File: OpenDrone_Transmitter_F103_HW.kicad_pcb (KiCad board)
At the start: 2 copper layers, 62 x 37 mm, 87 parts, among them J1 Conn_01x03, J10 Conn_01x04, J11 Conn_01x03, J12 Conn_01x04, J13 Conn_01x02, J14 Conn_01x05, J15 Conn_01x02, J16 Conn_02x04_Odd_Even, J17 Conn_01x02, J18 Conn_01x02, J19 Conn_01x03, J2 Conn_01x05, J20 Conn_01x02, J21 Conn_01x02, J22 Conn_01x02, J23 Conn_01x08, J3 Conn_01x03, J4 Conn_01x03, J5 Conn_01x03, J6 Conn_01x02, J7 Conn_01x02, J8 Conn_01x03, J9 Conn_01x03, SW1 RESET, U1 STM32F103C8Tx, U2 AMS1117-3.3, U3 TPS54331, Y2 Crystal_GND24

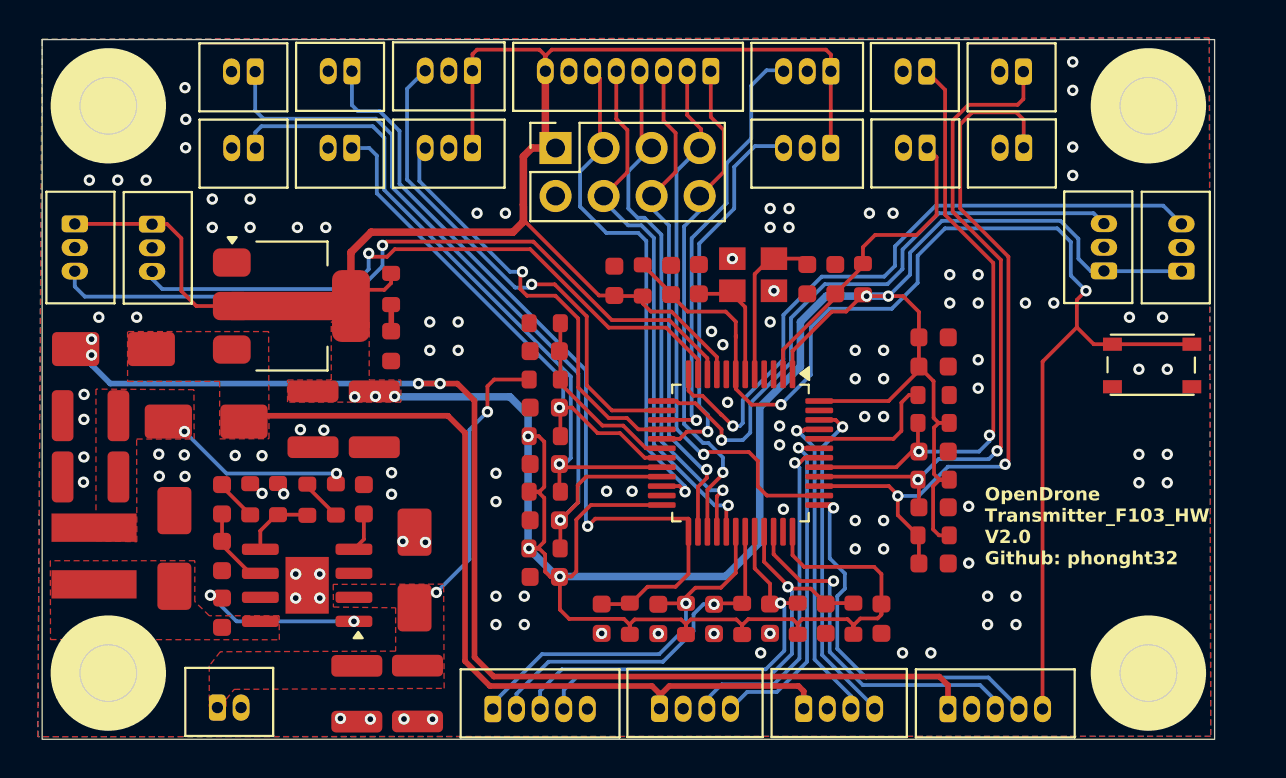
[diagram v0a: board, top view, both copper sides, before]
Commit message: update board size
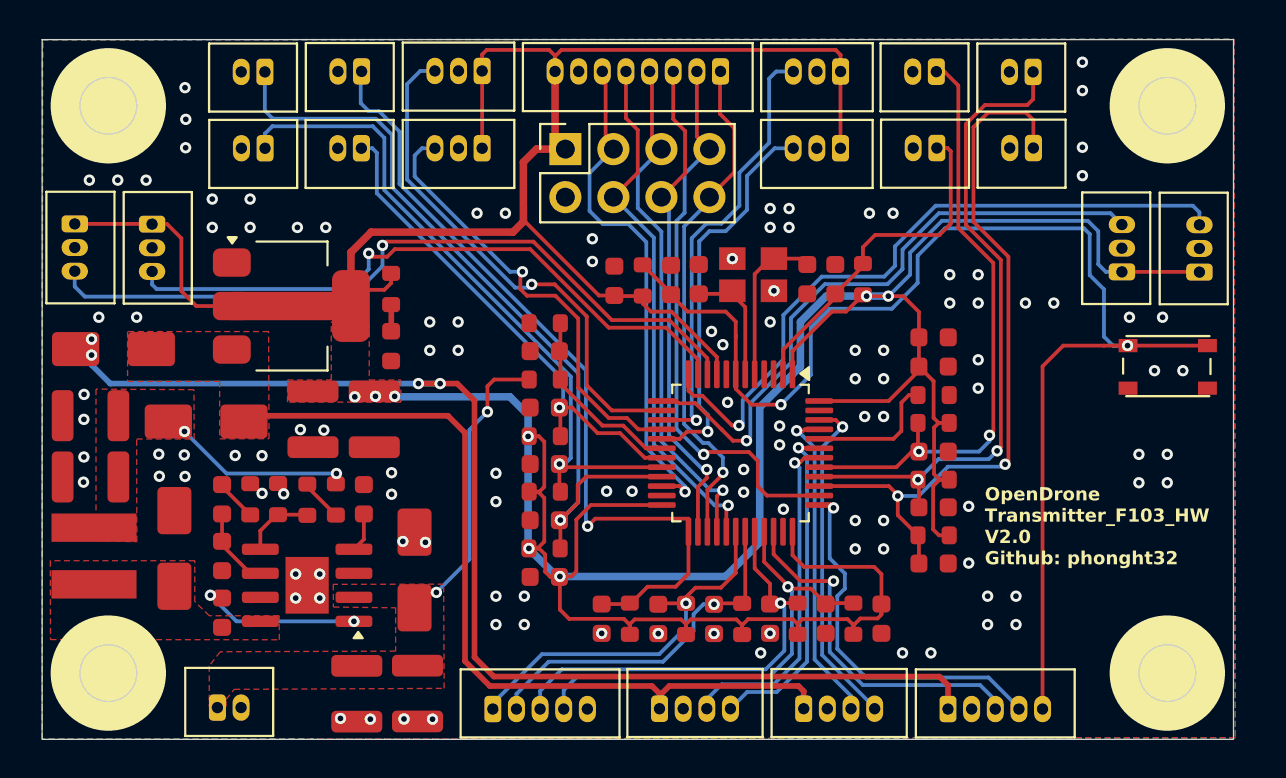
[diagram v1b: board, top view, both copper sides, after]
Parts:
- moved J19 0.95 mm to (224.7, 84.4)
- moved J5 0.95 mm to (220.6, 84.3)
- moved SW1 0.83 mm to (223.0, 89.4)
- moved J16 0.52 mm to (191.2, 77.9)
- moved J1 0.51 mm to (205.7, 73.8)
- moved J15 0.51 mm to (215.9, 73.8)
- moved J21 0.51 mm to (215.9, 77.8)
- moved J22 0.51 mm to (210.8, 77.8)
- moved J23 0.51 mm to (199.4, 73.8)
- moved J6 0.51 mm to (180.4, 73.8)
- moved J13 0.51 mm to (175.3, 77.8)
- moved J18 0.51 mm to (210.8, 73.8)
- moved J8 0.51 mm to (186.8, 73.7)
- moved J9 0.51 mm to (186.8, 77.8)
- moved J17 0.51 mm to (175.3, 73.8)
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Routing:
- net STM32_RESET: track 66.9 -> 69.8 mm
- net +3V3: track 240.6 -> 242.3 mm
- net PC13: track 16.7 -> 18.1 mm
- net RIGHT_JOYSTICK_IN1: track 35.6 -> 37.0 mm
- net VOLUME_3: track 23.0 -> 23.8 mm
- net RIGHT_JOYSTICK_IN2: track 32.7 -> 33.5 mm
- net VOLUME_1: track 27.0 -> 27.6 mm
- net VOLUME_2: track 23.0 -> 23.6 mm
- net NRF24_CE: track 28.7 -> 28.1 mm
- net PB4: track 35.9 -> 35.3 mm
- net PB3: track 39.2 -> 38.6 mm
- net PB12: track 43.6 -> 43.1 mm
- net PB2: track 36.7 -> 36.2 mm
- net PB10: track 43.1 -> 42.5 mm
- net GND: vias 112 -> 116
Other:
- board size 62 x 37 mm -> 63 x 37 mm
